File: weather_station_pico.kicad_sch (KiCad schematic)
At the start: 6 parts

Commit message: update sch
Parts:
- Q?: value (none) -> BSS138; footprint (none) -> Package_TO_SOT_SMD:SOT-23
- Q?: value (none) -> AO3401A; footprint (none) -> Package_TO_SOT_SMD:SOT-23
- U?: value (none) -> ADS1115IDGS; footprint (none) -> Package_SO:TSSOP-10_3x3mm_P0.5mm
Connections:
- net GND: now also U?.13 (GND), U?.3 (GND), U?.42 (GND), U?.8 (GND)
- net SCL: now reaches Q?.2 (S)
- net SDA_3V3: now reaches U?.26 (GPIO20)
- net SCL_3V3: now reaches U?.27 (GPIO21)
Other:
- moved on the sheet: Q?
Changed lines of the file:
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@@
   (junction (at 176.53 99.06) (diameter 0) (color 0 0 0 0)
   )
+  (wire (pts (xy 69.85 110.49) (xy 83.82 110.49))
+    (stroke (width 0) (type default) (color 0 0 0 0))
+  )
+  (wire (pts (xy 69.85 123.19) (xy 83.82 123.19))
+    (stroke (width 0) (type default) (color 0 0 0 0))
+  )
   (wire (pts (xy 176.53 83.82) (xy 176.53 86.36))
     (stroke (width 0) (type default) (color 0 0 0 0))
   )
-  (wire (pts (xy 163.83 91.44) (xy 168.91 91.44))
+  (wire (pts (xy 160.02 91.44) (xy 168.91 91.44))
+    (stroke (width 0) (type default) (color 0 0 0 0))
+  )
+  (wire (pts (xy 119.38 125.73) (xy 134.62 125.73))
+    (stroke (width 0) (type default) (color 0 0 0 0))
+  )
+  (wire (pts (xy 119.38 128.27) (xy 134.62 128.27))
+    (stroke (width 0) (type default) (color 0 0 0 0))
+  )
+  (wire (pts (xy 198.12 63.5) (xy 209.55 63.5))
     (stroke (width 0) (type default) (color 0 0 0 0))
   )
@@
     (stroke (width 0) (type default) (color 0 0 0 0))
   )
+  (wire (pts (xy 69.85 97.79) (xy 83.82 97.79))
+    (stroke (width 0) (type default) (color 0 0 0 0))
+  )
   (wire (pts (xy 83.82 135.89) (xy 69.85 135.89))
     (stroke (width 0) (type default) (color 0 0 0 0))
@@
     (stroke (width 0) (type default) (color 0 0 0 0))
   )
-  (wire (pts (xy 176.53 99.06) (xy 163.83 99.06))
-    (stroke (width 0) (type default) (color 0 0 0 0))
-  )
   (wire (pts (xy 119.38 95.25) (xy 134.62 95.25))
     (stroke (width 0) (type default) (color 0 0 0 0))
   )
-  (wire (pts (xy 69.85 135.89) (xy 69.85 139.7))
-    (stroke (width 0) (type default) (color 0 0 0 0))
+  (wire (pts (xy 160.02 99.06) (xy 176.53 99.06))
+    (stroke (width 0) (type default) (color 0 0 0 0))
+  )
+  (wire (pts (xy 101.6 146.05) (xy 101.6 152.4))
+    (stroke (width 0) (type default) (color 0 0 0 0))
+  )
+  (label "SCL" (at 198.12 63.5 180)
+    (effects (font (size 1.27 1.27)) (justify right bottom))
   )
   (label "VSYS" (at 134.62 95.25 180)
     (effects (font (size 1.27 1.27)) (justify right bottom))
   )
-  (label "VBUS" (at 163.83 91.44 0)
+  (label "SCL_3V3" (at 134.62 125.73 180)
+    (effects (font (size 1.27 1.27)) (justify right bottom))
+  )
+  (label "VBUS" (at 160.02 91.44 0)
     (effects (font (size 1.27 1.27)) (justify left bottom))
   )
-  (label "VSYS" (at 163.83 99.06 0)
+  (label "VSYS" (at 160.02 99.06 0)
     (effects (font (size 1.27 1.27)) (justify left bottom))
   )
@@
     (effects (font (size 1.27 1.27)) (justify right bottom))
   )
-  (symbol (lib_id "Transistor_FET:BSS138") (at 213.36 77.47 270) (unit 1)
-    (in_bom yes) (on_board yes) (fields_autoplaced)
-    (property "Reference" "Q?" (id 0) (at 213.36 83.9454 90))
-    (property "Value" "" (id 1) (at 213.36 86.4823 90))
-    (property "Footprint" "" (id 2) (at 211.455 82.55 0)
+  (label "SDA_3V3" (at 134.62 128.27 180)
+    (effects (font (size 1.27 1.27)) (justify right bottom))
+  )
+  (symbol (lib_id "Transistor_FET:BSS138") (at 214.63 60.96 270) (unit 1)
+    (in_bom yes) (on_board yes) (fields_autoplaced)
+    (property "Reference" "Q?" (id 0) (at 214.63 67.4354 90))
+    (property "Value" "BSS138" (id 1) (at 214.63 69.9723 90))
+    (property "Footprint" "Package_TO_SOT_SMD:SOT-23" (id 2) (at 212.725 66.04 0)
       (effects (font (size 1.27 1.27) italic) (justify left) hide)
     )
-    (property "Datasheet" "https://www.onsemi.com/pub/Collateral/BSS138-D.PDF" (id 3) (at 213.36 77.47 0)
+    (property "Datasheet" "https://www.onsemi.com/pub/Collateral/BSS138-D.PDF" (id 3) (at 214.63 60.96 0)
       (effects (font (size 1.27 1.27)) (justify left) hide)
     )
@@
     (pin "1")
   )
-  (symbol (lib_id "Transistor_FET:BSS138") (at 233.68 77.47 270) (unit 1)
-    (in_bom yes) (on_board yes) (fields_autoplaced)
-    (property "Reference" "Q?" (id 0) (at 233.68 83.9454 90))
-    (property "Value" "BSS138" (id 1) (at 233.68 86.4823 90))
-    (property "Footprint" "Package_TO_SOT_SMD:SOT-23" (id 2) (at 231.775 82.55 0)
+  (symbol (lib_id "Transistor_FET:BSS138") (at 247.65 60.96 270) (unit 1)
+    (in_bom yes) (on_board yes) (fields_autoplaced)
+    (property "Reference" "Q?" (id 0) (at 247.65 67.4354 90))
+    (property "Value" "BSS138" (id 1) (at 247.65 69.9723 90))
+    (property "Footprint" "Package_TO_SOT_SMD:SOT-23" (id 2) (at 245.745 66.04 0)
       (effects (font (size 1.27 1.27) italic) (justify left) hide)
     )
-    (property "Datasheet" "https://www.onsemi.com/pub/Collateral/BSS138-D.PDF" (id 3) (at 233.68 77.47 0)
+    (property "Datasheet" "https://www.onsemi.com/pub/Collateral/BSS138-D.PDF" (id 3) (at 247.65 60.96 0)
       (effects (font (size 1.27 1.27)) (justify left) hide)
     )
@@
     (pin "2")
     (pin "3")
+  )
+  (symbol (lib_id "power:GND") (at 69.85 97.79 270) (unit 1)
+    (in_bom yes) (on_board yes)
+    (property "Reference" "#PWR?" (id 0) (at 63.5 97.79 0)
+      (effects (font (size 1.27 1.27)) hide)
+    )
+    (property "Value" "GND" (id 1) (at 66.04 97.79 90)
+      (effects (font (size 1.27 1.27)) (justify right))
+    )
+    (property "Footprint" "" (id 2) (at 69.85 97.79 0)
+      (effects (font (size 1.27 1.27)) hide)
+    )
+    (property "Datasheet" "" (id 3) (at 69.85 97.79 0)
+      (effects (font (size 1.27 1.27)) hide)
+    )
+    (pin "1")
+  )
+  (symbol (lib_id "power:GND") (at 101.6 152.4 0) (unit 1)
+    (in_bom yes) (on_board yes) (fields_autoplaced)
+    (property "Reference" "#PWR?" (id 0) (at 101.6 158.75 0)
+      (effects (font (size 1.27 1.27)) hide)
+    )
+    (property "Value" "GND" (id 1) (at 101.6 156.8434 0))
+    (property "Footprint" "" (id 2) (at 101.6 152.4 0)
+      (effects (font (size 1.27 1.27)) hide)
+    )
+    (property "Datasheet" "" (id 3) (at 101.6 152.4 0)
+      (effects (font (size 1.27 1.27)) hide)
+    )
+    (pin "1")
   )
   (symbol (lib_id "Analog_ADC:ADS1115IDGS") (at 214.63 123.19 0) (unit 1)
@@
       (effects (font (size 1.27 1.27)) (justify left))
     )
-    (property "Value" "" (id 1) (at 216.6494 111.8671 0)
+    (property "Value" "ADS1115IDGS" (id 1) (at 216.6494 111.8671 0)
       (effects (font (size 1.27 1.27)) (justify left))
     )
-    (property "Footprint" "" (id 2) (at 214.63 135.89 0)
+    (property "Footprint" "Package_SO:TSSOP-10_3x3mm_P0.5mm" (id 2) (at 214.63 135.89 0)
       (effects (font (size 1.27 1.27)) hide)
     )
@@
     (pin "9")
   )
+  (symbol (lib_id "power:GND") (at 69.85 123.19 270) (unit 1)
+    (in_bom yes) (on_board yes)
+    (property "Reference" "#PWR?" (id 0) (at 63.5 123.19 0)
+      (effects (font (size 1.27 1.27)) hide)
+    )
+    (property "Value" "GND" (id 1) (at 66.04 123.19 90)
+      (effects (font (size 1.27 1.27)) (justify right))
+    )
+    (property "Footprint" "" (id 2) (at 69.85 123.19 0)
+      (effects (font (size 1.27 1.27)) hide)
+    )
+    (property "Datasheet" "" (id 3) (at 69.85 123.19 0)
+      (effects (font (size 1.27 1.27)) hide)
+    )
+    (pin "1")
+  )
   (symbol (lib_id "power:GND") (at 63.5 55.88 0) (unit 1)
     (in_bom yes) (on_board yes) (fields_autoplaced)
@@
       (effects (font (size 1.27 1.27)) (justify left))
     )
-    (property "Value" "" (id 1) (at 179.197 93.1422 0)
+    (property "Value" "AO3401A" (id 1) (at 179.197 93.1422 0)
       (effects (font (size 1.27 1.27)) (justify left))
     )
-    (property "Footprint" "" (id 2) (at 179.07 93.345 0)
+    (property "Footprint" "Package_TO_SOT_SMD:SOT-23" (id 2) (at 179.07 93.345 0)
       (effects (font (size 1.27 1.27) italic) (justify left) hide)
     )
@@
     (pin "3")
   )
-  (symbol (lib_id "power:GND") (at 69.85 139.7 0) (unit 1)
-    (in_bom yes) (on_board yes) (fields_autoplaced)
-    (property "Reference" "#PWR?" (id 0) (at 69.85 146.05 0)
-      (effects (font (size 1.27 1.27)) hide)
-    )
-    (property "Value" "GND" (id 1) (at 69.85 144.1434 0))
-    (property "Footprint" "" (id 2) (at 69.85 139.7 0)
-      (effects (font (size 1.27 1.27)) hide)
-    )
-    (property "Datasheet" "" (id 3) (at 69.85 139.7 0)
+  (symbol (lib_id "power:GND") (at 69.85 110.49 270) (unit 1)
+    (in_bom yes) (on_board yes)
+    (property "Reference" "#PWR?" (id 0) (at 63.5 110.49 0)
+      (effects (font (size 1.27 1.27)) hide)
+    )
+    (property "Value" "GND" (id 1) (at 66.04 110.49 90)
+      (effects (font (size 1.27 1.27)) (justify right))
+    )
+    (property "Footprint" "" (id 2) (at 69.85 110.49 0)
+      (effects (font (size 1.27 1.27)) hide)
+    )
+    (property "Datasheet" "" (id 3) (at 69.85 110.49 0)
+      (effects (font (size 1.27 1.27)) hide)
+    )
+    (pin "1")
+  )
+  (symbol (lib_id "power:GND") (at 69.85 135.89 270) (unit 1)
+    (in_bom yes) (on_board yes)
+    (property "Reference" "#PWR?" (id 0) (at 63.5 135.89 0)
+      (effects (font (size 1.27 1.27)) hide)
+    )
+    (property "Value" "" (id 1) (at 66.04 135.89 90)
+      (effects (font (size 1.27 1.27)) (justify right))
+    )
+    (property "Footprint" "" (id 2) (at 69.85 135.89 0)
+      (effects (font (size 1.27 1.27)) hide)
+    )
+    (property "Datasheet" "" (id 3) (at 69.85 135.89 0)
       (effects (font (size 1.27 1.27)) hide)
     )
@@
       (reference "#PWR?") (unit 1) (value "GND") (footprint "")
     )
+    (path "/7956a824-9c0b-49dc-83d1-077dcdb71882"
+      (reference "#PWR?") (unit 1) (value "GND") (footprint "")
+    )
+    (path "/86292fc3-6883-4ad4-abac-0fcfd4ef342c"
+      (reference "#PWR?") (unit 1) (value "GND") (footprint "")
+    )
+    (path "/b4409833-7b55-43a1-a013-652622484059"
+      (reference "#PWR?") (unit 1) (value "GND") (footprint "")
+    )
     (path "/bfbc4ccc-efbb-452f-8ca3-3c776d261a8a"
       (reference "#PWR?") (unit 1) (value "GND") (footprint "")
@@
       (reference "#PWR?") (unit 1) (value "+5V") (footprint "")
     )
+    (path "/f41dd84e-6491-406d-a2ce-1f6531fdae11"
+      (reference "#PWR?") (unit 1) (value "GND") (footprint "")
+    )
     (path "/fd06c2e8-ae40-46c0-9b3f-a158ea16c0a1"

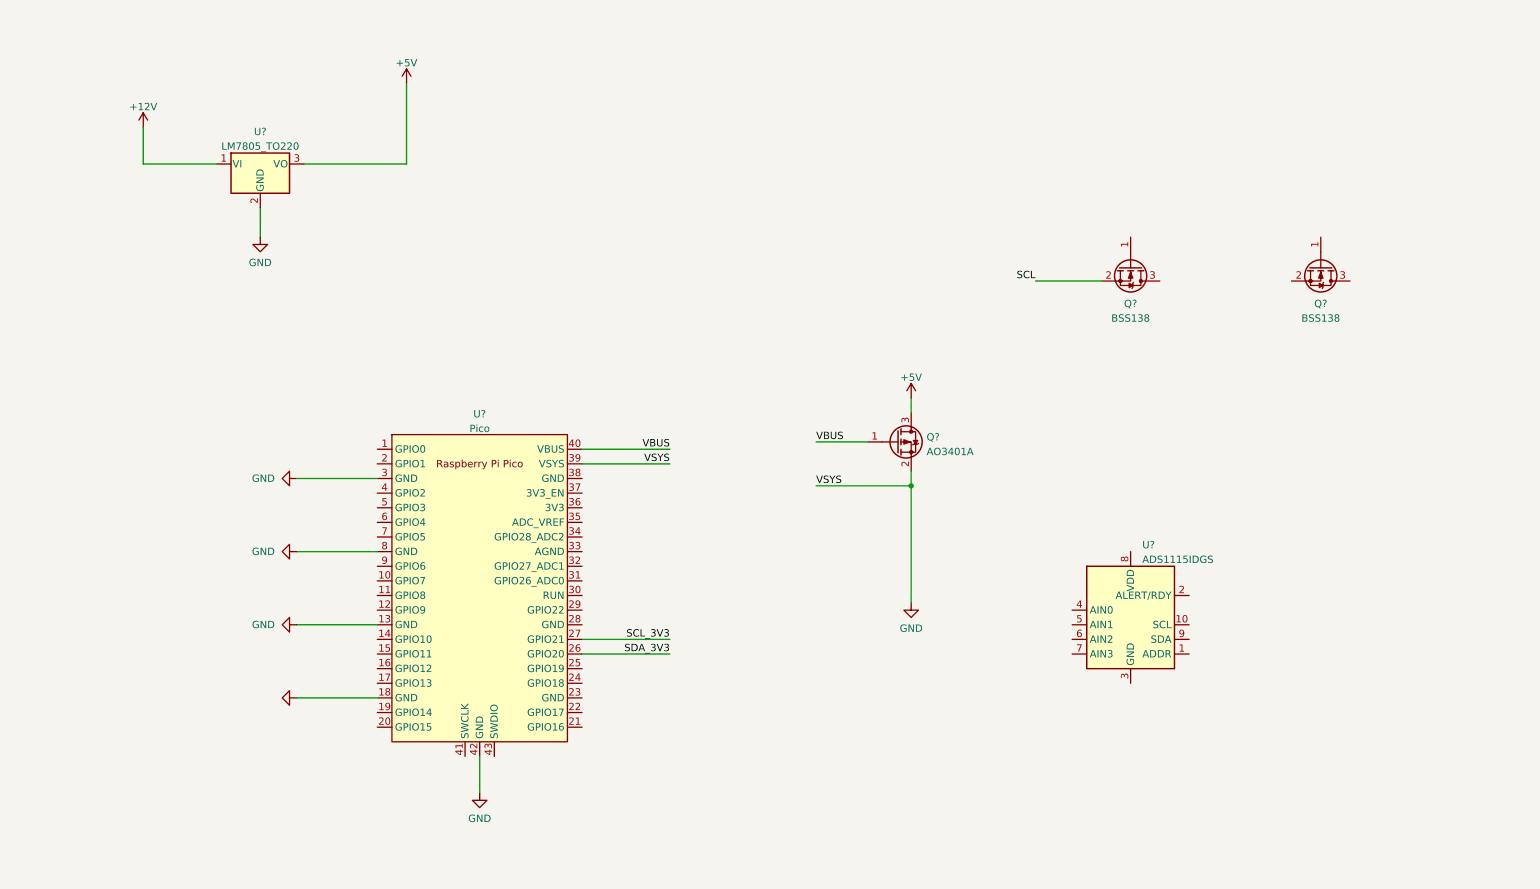
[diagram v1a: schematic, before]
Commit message: add some wires
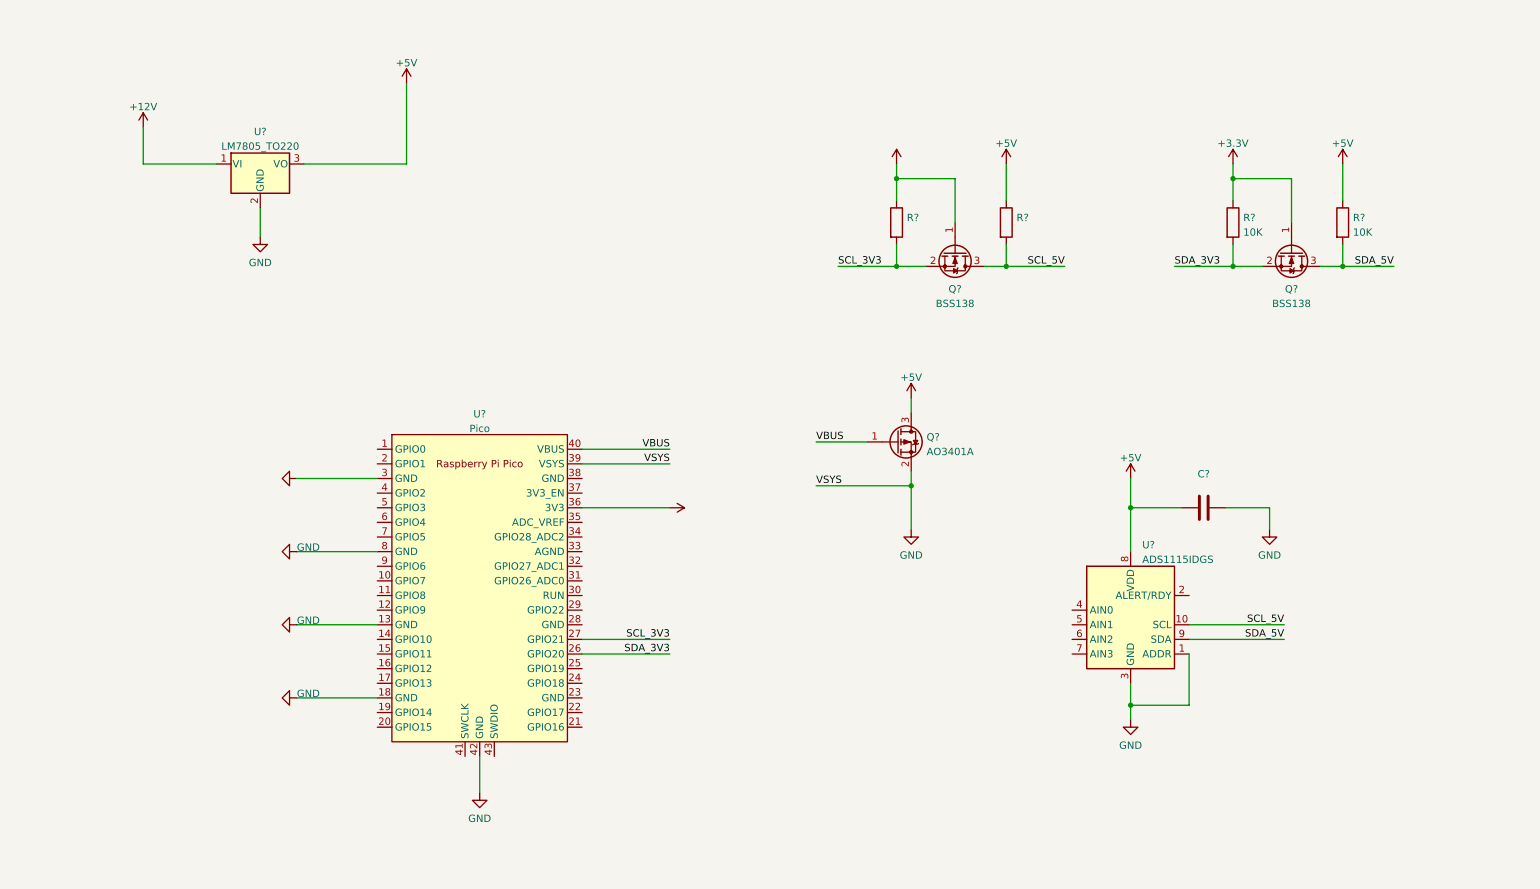
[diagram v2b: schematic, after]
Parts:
- removed Q?: BSS138, Package_TO_SOT_SMD:SOT-23, symbol Transistor_FET:BSS138
- added C?: (no value), symbol Device:C
- added Q?: BSS138, Package_TO_SOT_SMD:SOT-23, symbol Transistor_FET:BSS138
- added R? (x2): 10K, symbol Device:R
- added R? (x2): (no value), symbol Device:R
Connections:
- net SCL is gone; now on net SCL_3V3: Q?.2 (S)
- net +5V: now also U?.8 (VDD), C?.2, R?.1, R?.1
- net GND: now also U?.1 (ADDR), U?.3 (GND), C?.1
- net SCL_3V3: now also R?.2
- net SDA_3V3: now also Q?.2 (S), R?.2
- net +3V3: now reaches Q?.1 (G)
- net +3V3: now also U?.36 (3V3), Q?.1 (G), R?.1, R?.1
- net SCL_5V: now reaches Q?.3 (D)
- net SCL_5V: now also U?.10 (SCL), R?.2
- net SDA_5V: now reaches U?.9 (SDA)
- net SDA_5V: now also Q?.3 (D), R?.2
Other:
- moved on the sheet: Q?

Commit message: VSYS
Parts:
- removed C?: (no value), symbol Device:C
- added Q?: BSS138, Package_TO_SOT_SMD:SOT-23, symbol Transistor_FET:BSS138
- added R? (x2): 10K, symbol Device:R
- R? (x2): value (none) -> 10K
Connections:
- net +3V3: now also Q?.1 (G), R?.1
- net +5V: no longer R?.1, R?.1, U?.8 (VDD)
- net GND: now also R?.1, R?.1, U?.8 (VDD), R?.1
- net ALERT_3V3: now reaches U?.29 (GPIO22)
- net ALERT_3V3: now also Q?.2 (S), R?.2
- net ALERT_5V: now reaches U?.2 (ALERT/RDY)
- net ALERT_5V: now also Q?.3 (D), R?.2
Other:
- note added: "NOTA: tra VBUS e VSYS è presente un diodo MBR120VLSFT1G che può essere attraversato da 1A. La corrente passa nel diodo quando il circuito è alimentato da USB."
- moved on the sheet: Q?, R?
